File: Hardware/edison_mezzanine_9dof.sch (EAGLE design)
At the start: 35 parts, among them U1 LSM9DS0, U2 EDISON_CONNECTOR_FULLMOUNTING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, U3 EDISON_CONNECTOR_FULLHEADER

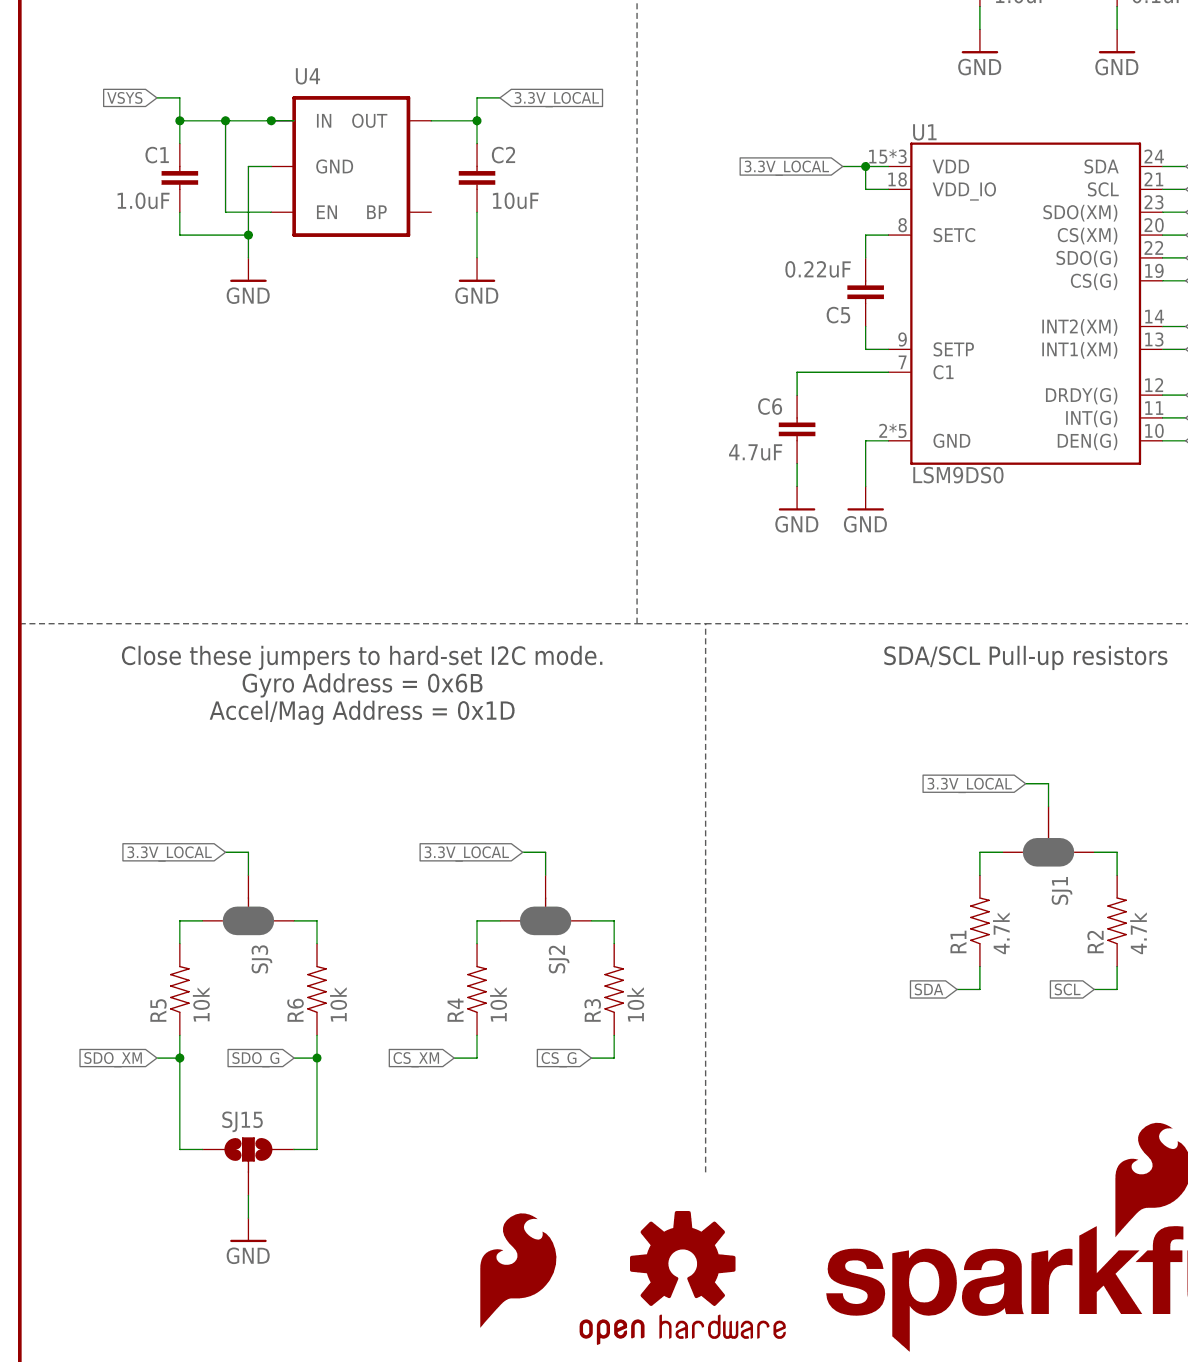
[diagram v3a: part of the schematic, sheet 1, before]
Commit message: Changed to 1.8V IO and added 4x 2-way jumpers for address select.
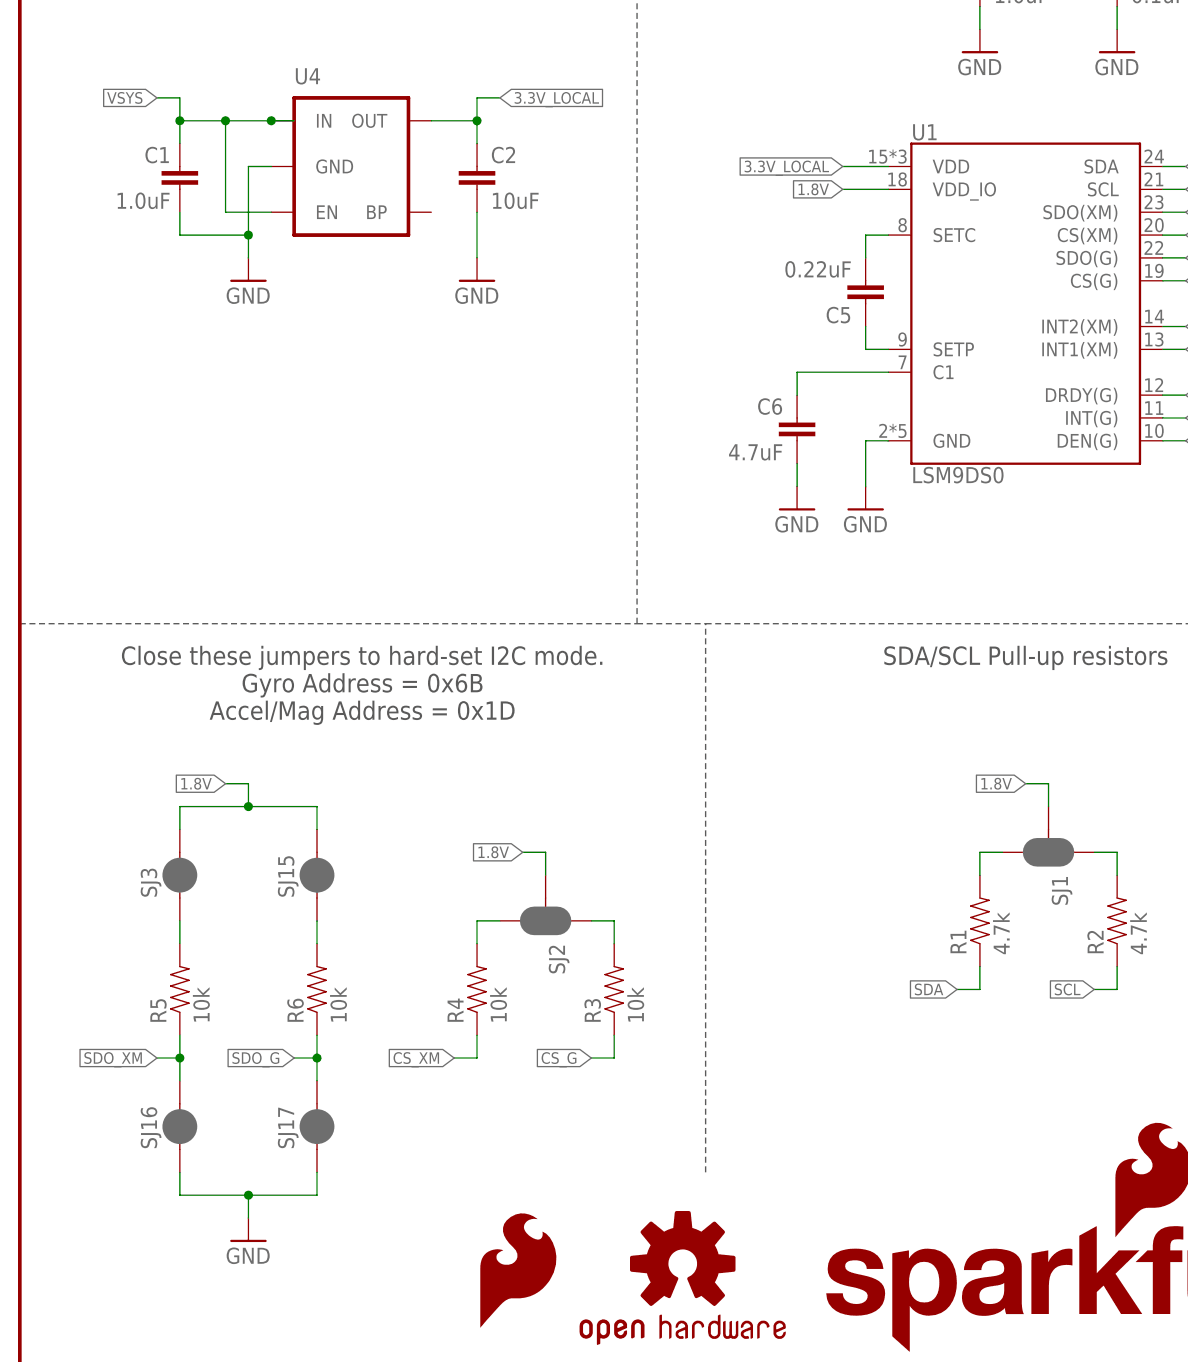
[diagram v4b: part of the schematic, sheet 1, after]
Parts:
- added SJ16, SJ17: JUMPER-PAD-2-NC_BY_PASTE, SparkFun-Passives:JUMPER-PAD-2-NC_BY_PASTE
- SJ15: value JUMPER-PAD-3-NOYES_SILK -> JUMPER-PAD-2-NC_BY_PASTE; device SparkFun-Passives:JUMPER-PAD-3-NOYES_SILK -> SparkFun-Passives:JUMPER-PAD-2-NC_BY_PASTE
- SJ3: value JUMPER-PAD-3-NC_BY_PASTE -> JUMPER-PAD-2-NC_BY_PASTE; device SparkFun-Passives:JUMPER-PAD-3-NC_BY_PASTE -> SparkFun-Passives:JUMPER-PAD-2-NC_BY_PASTE
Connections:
- net 1.8V: now also SJ1.2, SJ15.2, SJ2.2, SJ3.2, U1.VDD_IO
- net 3.3V_LOCAL: no longer SJ1.2, SJ2.2, SJ3.2, U1.VDD_IO
- net GND: now also SJ16.1, SJ17.1; no longer SJ15.2
- net N$12: now also SJ3.1; no longer SJ3.3
- net N$13: now also SJ15.1; no longer SJ3.1
- net SDO_G: now also SJ17.2; no longer SJ15.3
- net SDO_XM: now also SJ16.2; no longer SJ15.1
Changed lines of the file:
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@@
 <part name="SJ9" library="SparkFun-Passives" deviceset="JUMPER-PAD-3-2OF3_NC_BY_PASTE" device=""/>
 <part name="GND7" library="SparkFun-Aesthetics" deviceset="GND" device=""/>
-<part name="SJ15" library="SparkFun-Passives" deviceset="JUMPER-PAD-3-NO" device="YES_SILK"/>
-<part name="SJ3" library="SparkFun-Passives" deviceset="JUMPER-PAD-3-NC_BY_PASTE" device=""/>
 <part name="SJ2" library="SparkFun-Passives" deviceset="JUMPER-PAD-3-NC_BY_PASTE" device=""/>
 <part name="SJ1" library="SparkFun-Passives" deviceset="JUMPER-PAD-3-NC_BY_PASTE" device=""/>
@@
 <part name="GND8" library="SparkFun-Aesthetics" deviceset="GND" device=""/>
 <part name="GND9" library="SparkFun-Aesthetics" deviceset="GND" device=""/>
+<part name="SJ3" library="SparkFun-Passives" deviceset="JUMPER-PAD-2-NC_BY_PASTE" device=""/>
+<part name="SJ15" library="SparkFun-Passives" deviceset="JUMPER-PAD-2-NC_BY_PASTE" device=""/>
+<part name="SJ16" library="SparkFun-Passives" deviceset="JUMPER-PAD-2-NC_BY_PASTE" device=""/>
+<part name="SJ17" library="SparkFun-Passives" deviceset="JUMPER-PAD-2-NC_BY_PASTE" device=""/>
 </parts>
 <sheets>
@@
 </instance>
 <instance part="GND7" gate="1" x="25.4" y="15.24"/>
-<instance part="SJ15" gate="G$1" x="25.4" y="25.4" smashed="yes" rot="R90">
-<attribute name="NAME" x="22.352" y="27.813" size="1.778" layer="95"/>
-</instance>
-<instance part="SJ3" gate="G$1" x="25.4" y="50.8" smashed="yes" rot="R270">
-<attribute name="NAME" x="25.781" y="48.26" size="1.778" layer="95" rot="R270"/>
-</instance>
 <instance part="SJ2" gate="G$1" x="58.42" y="50.8" smashed="yes" rot="R270">
 <attribute name="NAME" x="58.801" y="48.26" size="1.778" layer="95" rot="R270"/>
@@
 <instance part="GND8" gate="1" x="25.4" y="121.92"/>
 <instance part="GND9" gate="1" x="50.8" y="121.92"/>
+<instance part="SJ3" gate="G$1" x="17.78" y="55.88" smashed="yes" rot="R90">
+<attribute name="NAME" x="15.24" y="53.34" size="1.778" layer="95" rot="R90"/>
+</instance>
+<instance part="SJ15" gate="G$1" x="33.02" y="55.88" smashed="yes" rot="R90">
+<attribute name="NAME" x="30.48" y="53.34" size="1.778" layer="95" rot="R90"/>
+</instance>
+<instance part="SJ16" gate="G$1" x="17.78" y="27.94" smashed="yes" rot="R90">
+<attribute name="NAME" x="15.24" y="25.4" size="1.778" layer="95" rot="R90"/>
+</instance>
+<instance part="SJ17" gate="G$1" x="33.02" y="27.94" smashed="yes" rot="R90">
+<attribute name="NAME" x="30.48" y="25.4" size="1.778" layer="95" rot="R90"/>
+</instance>
 </instances>
 <busses>
@@
 <wire x1="25.4" y1="20.32" x2="25.4" y2="17.78" width="0.1524" layer="91"/>
 <pinref part="GND7" gate="1" pin="GND"/>
-<pinref part="SJ15" gate="G$1" pin="2"/>
+<pinref part="SJ16" gate="G$1" pin="1"/>
+<wire x1="17.78" y1="22.86" x2="17.78" y2="20.32" width="0.1524" layer="91"/>
+<wire x1="17.78" y1="20.32" x2="25.4" y2="20.32" width="0.1524" layer="91"/>
+<pinref part="SJ17" gate="G$1" pin="1"/>
+<wire x1="33.02" y1="22.86" x2="33.02" y2="20.32" width="0.1524" layer="91"/>
+<wire x1="33.02" y1="20.32" x2="25.4" y2="20.32" width="0.1524" layer="91"/>
+<junction x="25.4" y="20.32"/>
 </segment>
 <segment>
@@
 <wire x1="33.02" y1="35.56" x2="30.48" y2="35.56" width="0.1524" layer="91"/>
 <label x="30.48" y="35.56" size="1.27" layer="95" rot="R180" xref="yes"/>
-<wire x1="30.48" y1="25.4" x2="33.02" y2="25.4" width="0.1524" layer="91"/>
-<wire x1="33.02" y1="25.4" x2="33.02" y2="35.56" width="0.1524" layer="91"/>
+<pinref part="SJ17" gate="G$1" pin="2"/>
+<wire x1="33.02" y1="35.56" x2="33.02" y2="33.02" width="0.1524" layer="91"/>
 <junction x="33.02" y="35.56"/>
-<pinref part="SJ15" gate="G$1" pin="3"/>
 </segment>
 <segment>
@@
 <wire x1="17.78" y1="35.56" x2="15.24" y2="35.56" width="0.1524" layer="91"/>
 <label x="15.24" y="35.56" size="1.27" layer="95" rot="R180" xref="yes"/>
-<wire x1="17.78" y1="35.56" x2="17.78" y2="25.4" width="0.1524" layer="91"/>
+<pinref part="SJ16" gate="G$1" pin="2"/>
+<wire x1="17.78" y1="35.56" x2="17.78" y2="33.02" width="0.1524" layer="91"/>
 <junction x="17.78" y="35.56"/>
-<wire x1="17.78" y1="25.4" x2="20.32" y2="25.4" width="0.1524" layer="91"/>
-<pinref part="SJ15" gate="G$1" pin="1"/>
 </segment>
 <segment>
@@
 <pinref part="R5" gate="G$1" pin="2"/>
 <wire x1="17.78" y1="48.26" x2="17.78" y2="50.8" width="0.1524" layer="91"/>
-<wire x1="17.78" y1="50.8" x2="20.32" y2="50.8" width="0.1524" layer="91"/>
-<pinref part="SJ3" gate="G$1" pin="3"/>
+<pinref part="SJ3" gate="G$1" pin="1"/>
 </segment>
 </net>
@@
 <segment>
 <pinref part="R6" gate="G$1" pin="2"/>
-<wire x1="30.48" y1="50.8" x2="33.02" y2="50.8" width="0.1524" layer="91"/>
 <wire x1="33.02" y1="50.8" x2="33.02" y2="48.26" width="0.1524" layer="91"/>
-<pinref part="SJ3" gate="G$1" pin="1"/>
+<pinref part="SJ15" gate="G$1" pin="1"/>
 </segment>
 </net>
@@
 </segment>
 <segment>
-<wire x1="25.4" y1="58.42" x2="25.4" y2="55.88" width="0.1524" layer="91"/>
+<pinref part="U1" gate="G$1" pin="VDD"/>
+<wire x1="96.52" y1="134.62" x2="91.44" y2="134.62" width="0.1524" layer="91"/>
+<label x="91.44" y="134.62" size="1.27" layer="95" rot="R180" xref="yes"/>
+</segment>
+</net>
+<net name="1.8V" class="0">
+<segment>
+<pinref part="U1" gate="G$1" pin="VDD_IO"/>
+<label x="91.44" y="132.08" size="1.27" layer="95" rot="R180" xref="yes"/>
+<wire x1="96.52" y1="132.08" x2="91.44" y2="132.08" width="0.1524" layer="91"/>
+</segment>
+<segment>
+<wire x1="25.4" y1="66.04" x2="25.4" y2="63.5" width="0.1524" layer="91"/>
+<wire x1="25.4" y1="66.04" x2="22.86" y2="66.04" width="0.1524" layer="91"/>
+<label x="22.86" y="66.04" size="1.27" layer="95" rot="R180" xref="yes"/>
 <pinref part="SJ3" gate="G$1" pin="2"/>
-<wire x1="25.4" y1="58.42" x2="22.86" y2="58.42" width="0.1524" layer="91"/>
-<label x="22.86" y="58.42" size="1.27" layer="95" rot="R180" xref="yes"/>
+<wire x1="17.78" y1="60.96" x2="17.78" y2="63.5" width="0.1524" layer="91"/>
+<wire x1="17.78" y1="63.5" x2="25.4" y2="63.5" width="0.1524" layer="91"/>
+<pinref part="SJ15" gate="G$1" pin="2"/>
+<wire x1="25.4" y1="63.5" x2="33.02" y2="63.5" width="0.1524" layer="91"/>
+<wire x1="33.02" y1="63.5" x2="33.02" y2="60.96" width="0.1524" layer="91"/>
+<junction x="25.4" y="63.5"/>
 </segment>
 <segment>
@@
 <label x="111.76" y="66.04" size="1.27" layer="95" rot="R180" xref="yes"/>
 </segment>
-<segment>
-<pinref part="U1" gate="G$1" pin="VDD"/>
-<wire x1="96.52" y1="134.62" x2="93.98" y2="134.62" width="0.1524" layer="91"/>
-<pinref part="U1" gate="G$1" pin="VDD_IO"/>
-<wire x1="96.52" y1="132.08" x2="93.98" y2="132.08" width="0.1524" layer="91"/>
-<wire x1="93.98" y1="132.08" x2="93.98" y2="134.62" width="0.1524" layer="91"/>
-<wire x1="93.98" y1="134.62" x2="91.44" y2="134.62" width="0.1524" layer="91"/>
-<junction x="93.98" y="134.62"/>
-<label x="91.44" y="134.62" size="1.27" layer="95" rot="R180" xref="yes"/>
-</segment>
-</net>
+</net>

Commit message: Re-did power section to include LDO. Added 4x 2-way jumpers to layout for pullups/pulldowns.
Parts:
- LOGO1: value SFE_LOGO_FLAME.3_INCH -> SFE_LOGO_FLAME.2_INCH; device SparkFun-Aesthetics:SFE_LOGO_FLAME.3_INCH -> SparkFun-Aesthetics:SFE_LOGO_FLAME.2_INCH
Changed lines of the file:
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@@
 <part name="SJ2" library="SparkFun-Passives" deviceset="JUMPER-PAD-3-NC_BY_PASTE" device=""/>
 <part name="SJ1" library="SparkFun-Passives" deviceset="JUMPER-PAD-3-NC_BY_PASTE" device=""/>
-<part name="LOGO1" library="SparkFun-Aesthetics" deviceset="SFE_LOGO_FLAME" device=".3_INCH"/>
 <part name="U4" library="SparkFun-PowerIC" deviceset="MIC5205" device="3.3V"/>
 <part name="C1" library="SparkFun-Capacitors" deviceset="1.0UF-16V-10%(0603)" device="" value="1.0uF"/>
@@
 <part name="SJ16" library="SparkFun-Passives" deviceset="JUMPER-PAD-2-NC_BY_PASTE" device=""/>
 <part name="SJ17" library="SparkFun-Passives" deviceset="JUMPER-PAD-2-NC_BY_PASTE" device=""/>
+<part name="LOGO1" library="SparkFun-Aesthetics" deviceset="SFE_LOGO_FLAME" device=".2_INCH"/>
 </parts>
 <sheets>
@@
 <instance part="FRAME1" gate="G$1" x="0" y="0"/>
 <instance part="FRAME1" gate="G$2" x="147.32" y="0"/>
-<instance part="LOGO2" gate="G$1" x="73.66" y="12.7"/>
+<instance part="LOGO2" gate="G$1" x="236.22" y="45.72"/>
 <instance part="LOGO3" gate="G$1" x="88.9" y="2.54"/>
 <instance part="U1" gate="G$1" x="111.76" y="119.38"/>
@@
 <attribute name="NAME" x="114.681" y="55.88" size="1.778" layer="95" rot="R270"/>
 </instance>
-<instance part="LOGO1" gate="G$1" x="50.8" y="5.08"/>
 <instance part="U4" gate="G$1" x="38.1" y="134.62"/>
 <instance part="C1" gate="G$1" x="17.78" y="132.08" smashed="yes">
@@
 <attribute name="NAME" x="30.48" y="25.4" size="1.778" layer="95" rot="R90"/>
 </instance>
+<instance part="LOGO1" gate="G$1" x="71.12" y="5.08"/>
 </instances>
 <busses>
